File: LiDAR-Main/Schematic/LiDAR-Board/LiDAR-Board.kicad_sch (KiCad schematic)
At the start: 9 parts, among them J1 Conn_01x04, Q1 NPN, Q2 NPN, U1 Pico

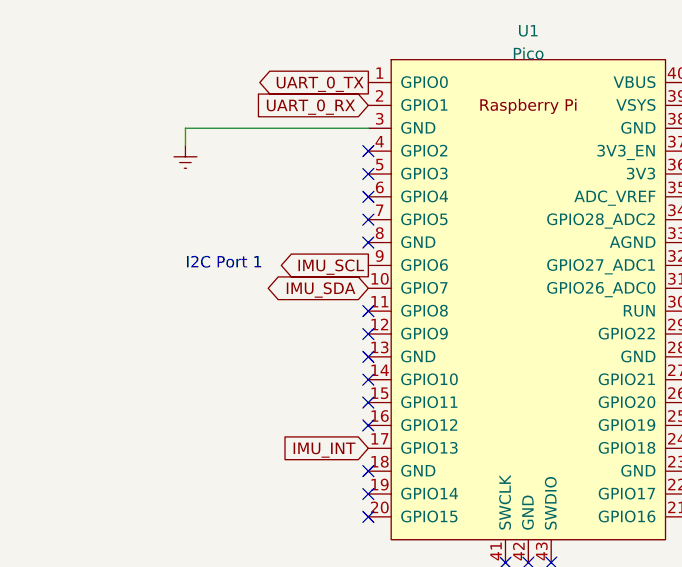
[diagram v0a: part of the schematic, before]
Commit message: Fixed IMU I2C Pin allocation
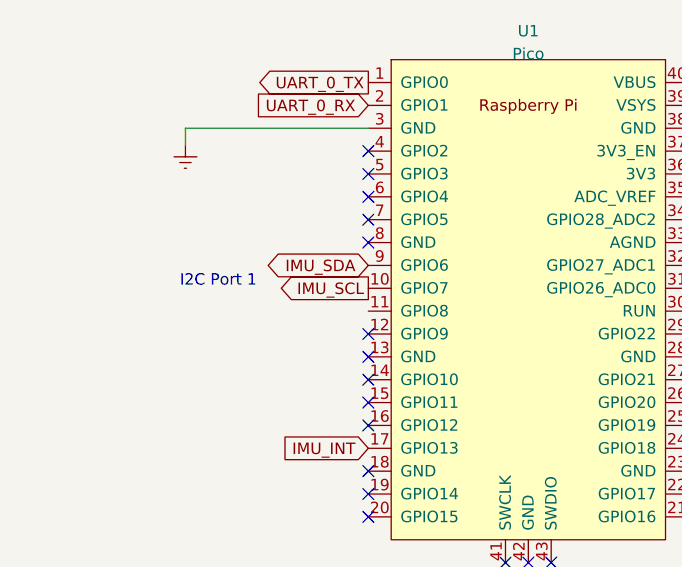
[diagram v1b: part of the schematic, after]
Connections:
- net IMU_SCL: now also U1.10 (GPIO7); no longer U1.9 (GPIO6)
- net IMU_SDA: now also U1.9 (GPIO6); no longer U1.10 (GPIO7)
- no-connect marks 30 -> 29
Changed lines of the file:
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@@
   (no_connect (at 78.74 127.635))
   (no_connect (at 93.98 104.775))
-  (no_connect (at 58.42 99.695))
   (no_connect (at 58.42 112.395))
   (no_connect (at 76.2 127.635))
@@
     (effects (font (size 1.27 1.27)) (justify left bottom))
   )
-  (text "I2C Port 1\n" (at 38.1 95.25 0)
+  (text "I2C Port 1\n" (at 37.465 97.155 0)
     (effects (font (size 1.27 1.27)) (justify left bottom))
   )
@@
     )
   )
-  (global_label "IMU_SDA" (shape bidirectional) (at 58.42 97.155 180) (fields_autoplaced)
-    (effects (font (size 1.27 1.27)) (justify right))
-    (property "Intersheetrefs" "${INTERSHEET_REFS}" (at 46.4805 97.155 0)
+  (global_label "IMU_SDA" (shape bidirectional) (at 58.42 94.615 180) (fields_autoplaced)
+    (effects (font (size 1.27 1.27)) (justify right))
+    (property "Intersheetrefs" "${INTERSHEET_REFS}" (at 46.4805 94.615 0)
       (effects (font (size 1.27 1.27)) (justify right) hide)
     )
@@
     )
   )
-  (global_label "IMU_SCL" (shape output) (at 58.42 94.615 180) (fields_autoplaced)
-    (effects (font (size 1.27 1.27)) (justify right))
-    (property "Intersheetrefs" "${INTERSHEET_REFS}" (at 47.6523 94.615 0)
-      (effects (font (size 1.27 1.27)) (justify right) hide)
-    )
+  (global_label "IMU_SCL" (shape output) (at 58.42 97.155 180) (fields_autoplaced)
+    (effects (font (size 1.27 1.27)) (justify right))
+    (property "Intersheetrefs" "${INTERSHEET_REFS}" (at 47.6523 97.155 0)
+      (effects (font (size 1.27 1.27)) (justify right) hide)
+    )

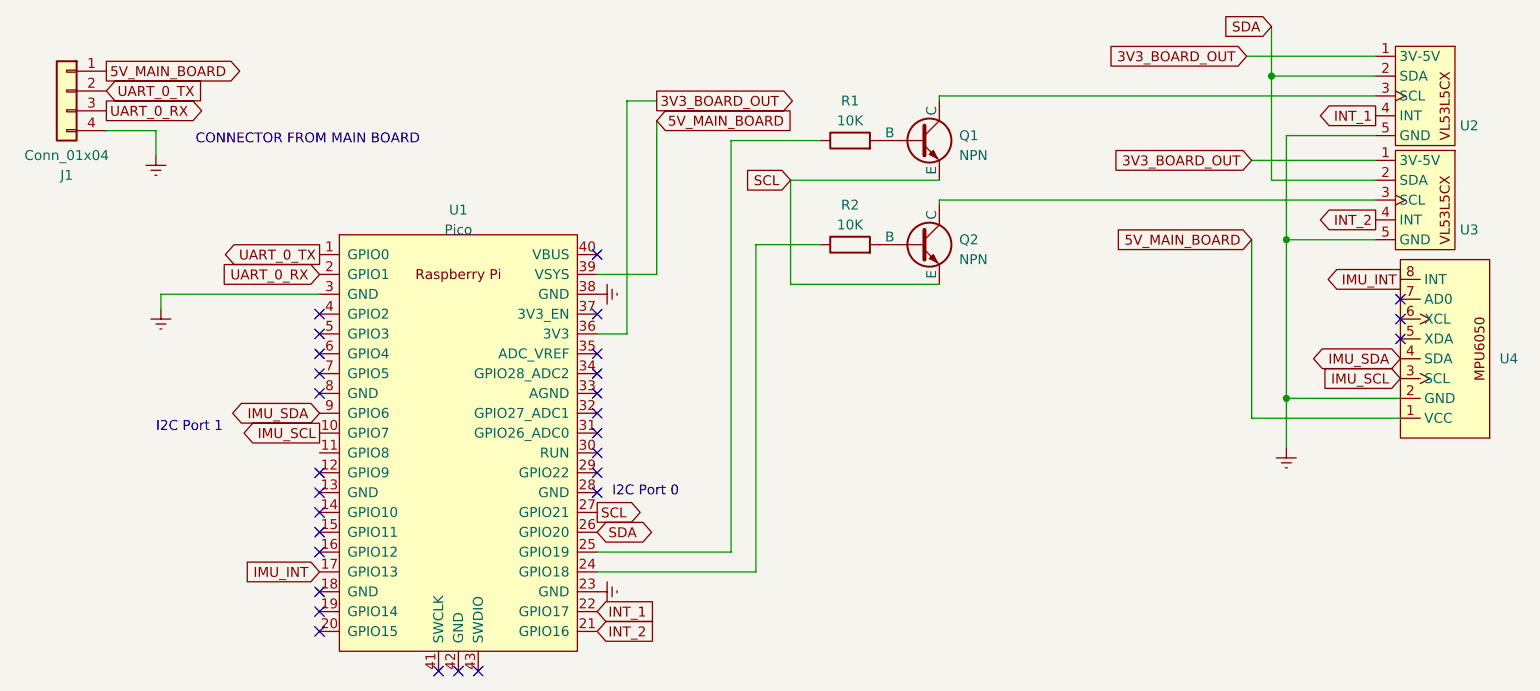
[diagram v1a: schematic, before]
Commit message: Corrected Tx/Rx assignment
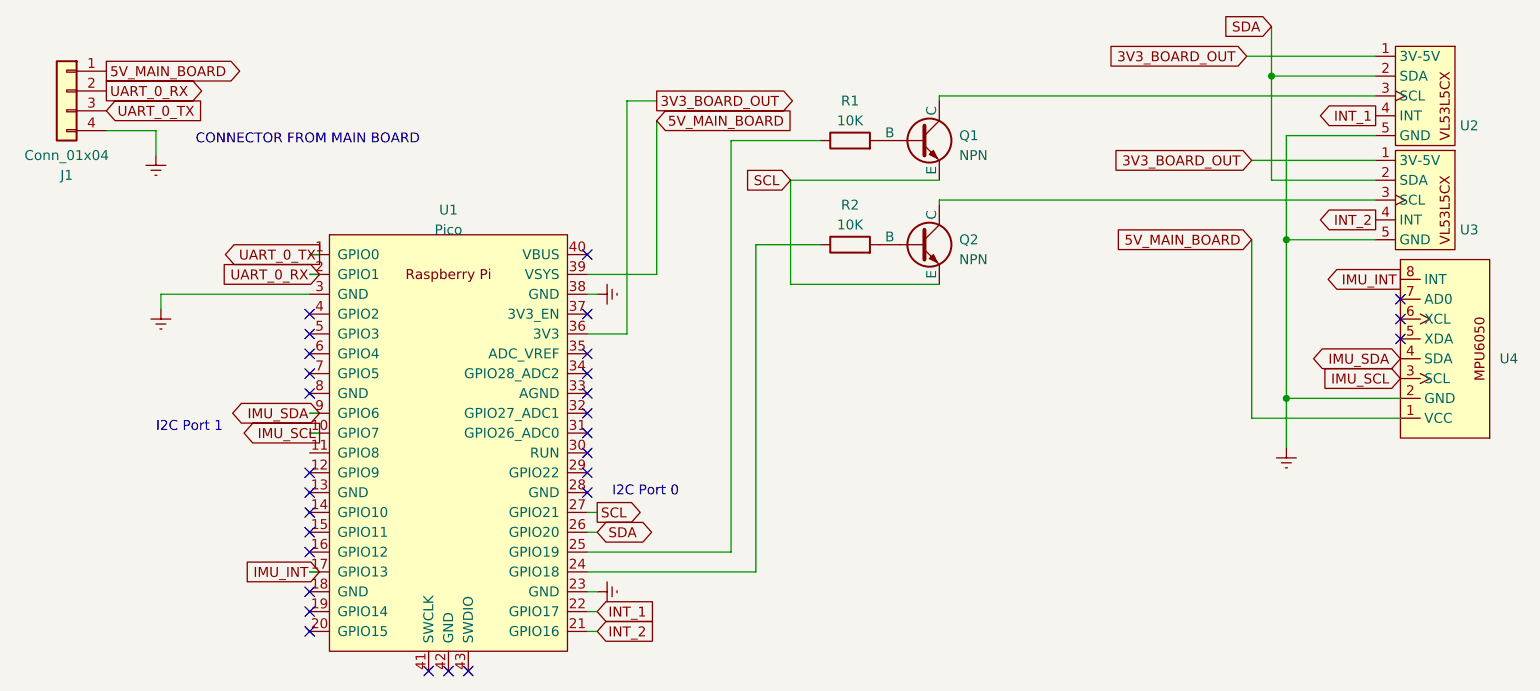
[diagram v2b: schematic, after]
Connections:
- net UART_0_RX: now also J1.2 (Pin_2); no longer J1.3 (Pin_3)
- net UART_0_TX: now also J1.3 (Pin_3); no longer J1.2 (Pin_2)
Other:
- moved on the sheet: U1
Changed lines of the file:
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@@
   (junction (at 182.245 72.39) (diameter 0) (color 0 0 0 0)
   )
-  (no_connect (at 58.42 120.015))
-  (no_connect (at 58.42 92.075))
-  (no_connect (at 58.42 81.915))
-  (no_connect (at 93.98 89.535))
+  (no_connect (at 57.15 120.015))
+  (no_connect (at 57.15 92.075))
+  (no_connect (at 57.15 81.915))
+  (no_connect (at 92.71 89.535))
   (no_connect (at 196.85 80.01))
-  (no_connect (at 93.98 102.235))
-  (no_connect (at 93.98 94.615))
-  (no_connect (at 93.98 99.695))
-  (no_connect (at 58.42 104.775))
-  (no_connect (at 93.98 97.155))
-  (no_connect (at 93.98 74.295))
-  (no_connect (at 58.42 109.855))
-  (no_connect (at 58.42 89.535))
-  (no_connect (at 93.98 86.995))
-  (no_connect (at 58.42 107.315))
+  (no_connect (at 92.71 102.235))
+  (no_connect (at 92.71 94.615))
+  (no_connect (at 92.71 99.695))
+  (no_connect (at 57.15 104.775))
+  (no_connect (at 92.71 97.155))
+  (no_connect (at 92.71 74.295))
+  (no_connect (at 57.15 109.855))
+  (no_connect (at 57.15 89.535))
+  (no_connect (at 92.71 86.995))
+  (no_connect (at 57.15 107.315))
   (no_connect (at 196.85 85.09))
-  (no_connect (at 78.74 127.635))
-  (no_connect (at 93.98 104.775))
-  (no_connect (at 58.42 112.395))
-  (no_connect (at 76.2 127.635))
-  (no_connect (at 73.66 127.635))
-  (no_connect (at 58.42 86.995))
-  (no_connect (at 58.42 102.235))
+  (no_connect (at 77.47 127.635))
+  (no_connect (at 92.71 104.775))
+  (no_connect (at 57.15 112.395))
+  (no_connect (at 74.93 127.635))
+  (no_connect (at 72.39 127.635))
+  (no_connect (at 57.15 86.995))
+  (no_connect (at 57.15 102.235))
   (no_connect (at 196.85 82.55))
-  (no_connect (at 58.42 84.455))
-  (no_connect (at 93.98 92.075))
-  (no_connect (at 93.98 81.915))
-  (no_connect (at 58.42 117.475))
-  (no_connect (at 58.42 122.555))
-  (wire (pts (xy 58.42 79.375) (xy 38.1 79.375))
+  (no_connect (at 57.15 84.455))
+  (no_connect (at 92.71 92.075))
+  (no_connect (at 92.71 81.915))
+  (no_connect (at 57.15 117.475))
+  (no_connect (at 57.15 122.555))
+  (wire (pts (xy 57.15 79.375) (xy 38.1 79.375))
     (stroke (width 0) (type default))
   )
@@
     (stroke (width 0) (type default))
   )
+  (wire (pts (xy 57.15 97.155) (xy 58.42 97.155))
+    (stroke (width 0) (type default))
+  )
   (wire (pts (xy 111.125 112.395) (xy 111.125 59.69))
     (stroke (width 0) (type default))
@@
     (stroke (width 0) (type default))
   )
+  (wire (pts (xy 57.15 74.295) (xy 58.42 74.295))
+    (stroke (width 0) (type default))
+  )
   (wire (pts (xy 114.3 73.025) (xy 114.3 114.935))
     (stroke (width 0) (type default))
@@
     (stroke (width 0) (type default))
   )
-  (wire (pts (xy 114.3 114.935) (xy 93.98 114.935))
+  (wire (pts (xy 57.15 114.935) (xy 58.42 114.935))
+    (stroke (width 0) (type default))
+  )
+  (wire (pts (xy 114.3 114.935) (xy 92.71 114.935))
     (stroke (width 0) (type default))
   )
@@
     (stroke (width 0) (type default))
   )
+  (wire (pts (xy 92.71 117.475) (xy 93.98 117.475))
+    (stroke (width 0) (type default))
+  )
   (wire (pts (xy 118.745 78.105) (xy 137.795 78.105))
     (stroke (width 0) (type default))
@@
     (stroke (width 0) (type default))
   )
-  (wire (pts (xy 93.98 112.395) (xy 111.125 112.395))
+  (wire (pts (xy 92.71 112.395) (xy 111.125 112.395))
     (stroke (width 0) (type default))
   )
@@
     (stroke (width 0) (type default))
   )
+  (wire (pts (xy 92.71 107.315) (xy 93.98 107.315))
+    (stroke (width 0) (type default))
+  )
   (wire (pts (xy 196.85 92.71) (xy 182.245 92.71))
     (stroke (width 0) (type default))
   )
+  (wire (pts (xy 92.71 122.555) (xy 93.98 122.555))
+    (stroke (width 0) (type default))
+  )
   (wire (pts (xy 177.165 48.895) (xy 193.675 48.895))
     (stroke (width 0) (type default))
@@
     (stroke (width 0) (type default))
   )
-  (wire (pts (xy 101.6 76.835) (xy 93.98 76.835))
+  (wire (pts (xy 101.6 76.835) (xy 92.71 76.835))
     (stroke (width 0) (type default))
   )
@@
     (stroke (width 0) (type default))
   )
+  (wire (pts (xy 92.71 109.855) (xy 93.98 109.855))
+    (stroke (width 0) (type default))
+  )
   (wire (pts (xy 180.34 51.435) (xy 180.34 64.77))
     (stroke (width 0) (type default))
@@
     (stroke (width 0) (type default))
   )
-  (wire (pts (xy 93.98 84.455) (xy 97.79 84.455))
+  (wire (pts (xy 92.71 84.455) (xy 97.79 84.455))
     (stroke (width 0) (type default))
   )
@@
     (stroke (width 0) (type default))
   )
+  (wire (pts (xy 57.15 94.615) (xy 58.42 94.615))
+    (stroke (width 0) (type default))
+  )
   (wire (pts (xy 180.34 51.435) (xy 193.675 51.435))
     (stroke (width 0) (type default))
@@
     (stroke (width 0) (type default))
   )
+  (wire (pts (xy 92.71 120.015) (xy 93.98 120.015))
+    (stroke (width 0) (type default))
+  )
   (wire (pts (xy 111.125 59.69) (xy 122.555 59.69))
+    (stroke (width 0) (type default))
+  )
+  (wire (pts (xy 92.71 79.375) (xy 93.98 79.375))
+    (stroke (width 0) (type default))
+  )
+  (wire (pts (xy 57.15 76.835) (xy 58.42 76.835))
     (stroke (width 0) (type default))
   )
@@
     )
   )
-  (global_label "UART_0_RX" (shape output) (at 31.115 55.88 0) (fields_autoplaced)
-    (effects (font (size 1.27 1.27)) (justify left))
-    (property "Intersheetrefs" "${INTERSHEET_REFS}" (at 44.3017 55.88 0)
+  (global_label "UART_0_RX" (shape output) (at 31.115 53.34 0) (fields_autoplaced)
+    (effects (font (size 1.27 1.27)) (justify left))
+    (property "Intersheetrefs" "${INTERSHEET_REFS}" (at 44.3017 53.34 0)
       (effects (font (size 1.27 1.27)) (justify left) hide)
     )
@@
     )
   )
-  (global_label "UART_0_TX" (shape input) (at 31.115 53.34 0) (fields_autoplaced)
-    (effects (font (size 1.27 1.27)) (justify left))
-    (property "Intersheetrefs" "${INTERSHEET_REFS}" (at 43.9993 53.34 0)
+  (global_label "UART_0_TX" (shape input) (at 31.115 55.88 0) (fields_autoplaced)
+    (effects (font (size 1.27 1.27)) (justify left))
+    (property "Intersheetrefs" "${INTERSHEET_REFS}" (at 43.9993 55.88 0)
       (effects (font (size 1.27 1.27)) (justify left) hide)
     )
@@
     )
   )
-  (symbol (lib_id "HEVCS_Sensors:Pico") (at 76.2 98.425 0) (unit 1)
-    (in_bom yes) (on_board yes) (dnp no) (fields_autoplaced)
-    (property "Reference" "U1" (at 76.2 68.58 0)
+  (symbol (lib_id "HEVCS_Sensors:Pico") (at 74.93 98.425 0) (unit 1)
+    (in_bom yes) (on_board yes) (dnp no) (fields_autoplaced)
+    (property "Reference" "U1" (at 74.93 68.58 0)
       (effects (font (size 1.27 1.27)))
     )
-    (property "Value" "Pico" (at 76.2 71.12 0)
+    (property "Value" "Pico" (at 74.93 71.12 0)
       (effects (font (size 1.27 1.27)))
     )
-    (property "Footprint" "HEVCS_Sensor_Footprints:Pi_Pico" (at 76.2 98.425 90)
-      (effects (font (size 1.27 1.27)) hide)
-    )
-    (property "Datasheet" "" (at 76.2 98.425 0)
-      (effects (font (size 1.27 1.27)) hide)
-    )
+    (property "Footprint" "HEVCS_Sensor_Footprints:Pi_Pico" (at 74.93 98.425 90)
+      (effects (font (size 1.27 1.27)) hide)
+    )
+    (property "Datasheet" "" (at 74.93 98.425 0)
+      (effects (font (size 1.27 1.27)) hide)
+    )

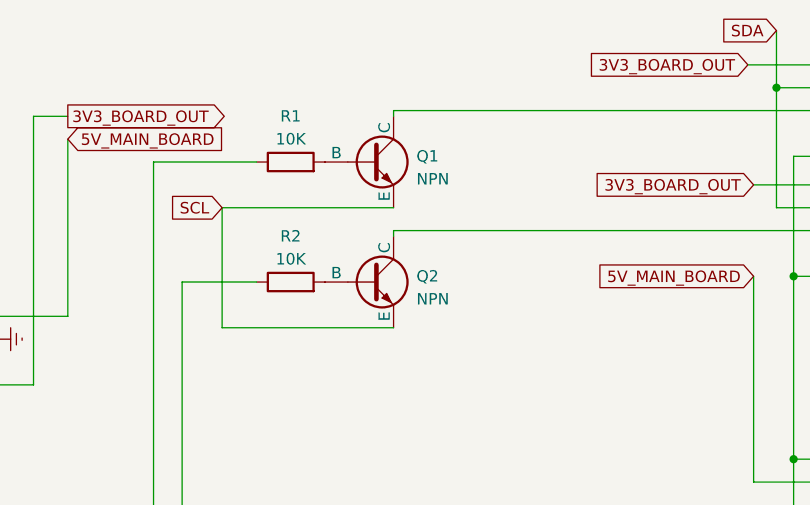
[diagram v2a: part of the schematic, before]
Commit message: Transistor footprint correction - BC817
Replaced generic transistor symbol with the BC817 in a SOT23 package.
Fixed footprint allocation and re-done PCB traces to accomodate change.
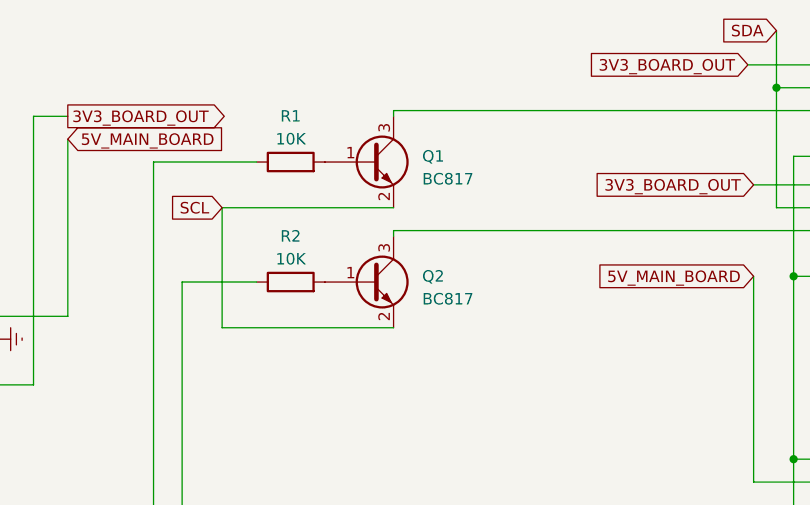
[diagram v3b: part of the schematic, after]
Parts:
- removed Q1, Q2: NPN, Package_TO_SOT_SMD:SOT-23, symbol Simulation_SPICE:NPN
- added Q1, Q2: BC817, Package_TO_SOT_SMD:SOT-23, symbol Transistor_BJT:BC817
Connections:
- net SCL: now also Q1.2 (E), Q2.2 (E)
- net at U2.3 (SCL): now also Q1.3 (C)
- net at R1.2: now also Q1.1 (B)
- net at U3.3 (SCL): now also Q2.3 (C)
- net at R2.2: now also Q2.1 (B)
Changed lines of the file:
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@@
-    )
-  )
-  (symbol (lib_id "Simulation_SPICE:NPN") (at 135.255 59.69 0) (unit 1)
-    (in_bom yes) (on_board yes) (dnp no) (fields_autoplaced)
-    (property "Reference" "Q1" (at 140.335 59.055 0)
-      (effects (font (size 1.27 1.27)) (justify left))
-    )
-    (property "Value" "NPN" (at 140.335 61.595 0)
-      (effects (font (size 1.27 1.27)) (justify left))
-    )
-    (property "Footprint" "Package_TO_SOT_SMD:SOT-23" (at 198.755 59.69 0)
-      (effects (font (size 1.27 1.27)) hide)
-    )
-    (property "Datasheet" "~" (at 198.755 59.69 0)
-      (effects (font (size 1.27 1.27)) hide)
-    )
-    (property "Sim.Device" "NPN" (at 135.255 59.69 0)
-      (effects (font (size 1.27 1.27)) hide)
-    )
-    (property "Sim.Type" "GUMMELPOON" (at 135.255 59.69 0)
-      (effects (font (size 1.27 1.27)) hide)
-    )
-    (property "Sim.Pins" "1=C 2=B 3=E" (at 135.255 59.69 0)
-      (effects (font (size 1.27 1.27)) hide)
-    )
-    (pin "1")
-    (pin "2")
-    (pin "3")
-    (instances
-      (project "LiDAR-Board"
-        (path "/379f291a-31d3-4ed1-aaf1-b1b6ffabef49"
-          (reference "Q1") (unit 1)
-        )
-      )
-    )
-  )
-  (symbol (lib_id "Simulation_SPICE:NPN") (at 135.255 73.025 0) (unit 1)
-    (in_bom yes) (on_board yes) (dnp no) (fields_autoplaced)
-    (property "Reference" "Q2" (at 140.335 72.39 0)
-      (effects (font (size 1.27 1.27)) (justify left))
-    )
-    (property "Value" "NPN" (at 140.335 74.93 0)
-      (effects (font (size 1.27 1.27)) (justify left))
-    )
-    (property "Footprint" "Package_TO_SOT_SMD:SOT-23" (at 198.755 73.025 0)
-      (effects (font (size 1.27 1.27)) hide)
-    )
-    (property "Datasheet" "~" (at 198.755 73.025 0)
-      (effects (font (size 1.27 1.27)) hide)
-    )
-    (property "Sim.Device" "NPN" (at 135.255 73.025 0)
-      (effects (font (size 1.27 1.27)) hide)
-    )
-    (property "Sim.Type" "GUMMELPOON" (at 135.255 73.025 0)
-      (effects (font (size 1.27 1.27)) hide)
-    )
-    (property "Sim.Pins" "1=C 2=B 3=E" (at 135.255 73.025 0)
-      (effects (font (size 1.27 1.27)) hide)
-    )
-    (pin "1")
-    (pin "2")
-    (pin "3")
-    (instances
-      (project "LiDAR-Board"
-        (path "/379f291a-31d3-4ed1-aaf1-b1b6ffabef49"
-          (reference "Q2") (unit 1)
-        )
-      )
     )
   )
@@
     )
   )
+  (symbol (lib_id "Transistor_BJT:BC817") (at 135.255 73.025 0) (unit 1)
+    (in_bom yes) (on_board yes) (dnp no) (fields_autoplaced)
+    (property "Reference" "Q2" (at 140.97 72.39 0)
+      (effects (font (size 1.27 1.27)) (justify left))
+    )
+    (property "Value" "BC817" (at 140.97 74.93 0)
+      (effects (font (size 1.27 1.27)) (justify left))
+    )
+    (property "Footprint" "Package_TO_SOT_SMD:SOT-23" (at 140.335 74.93 0)
+      (effects (font (size 1.27 1.27) italic) (justify left) hide)
+    )
+    (property "Datasheet" "https://www.onsemi.com/pub/Collateral/BC818-D.pdf" (at 135.255 73.025 0)
+      (effects (font (size 1.27 1.27)) (justify left) hide)
+    )
+    (pin "1")
+    (pin "2")
+    (pin "3")
+    (instances
+      (project "LiDAR-Board"
+        (path "/379f291a-31d3-4ed1-aaf1-b1b6ffabef49"
+          (reference "Q2") (unit 1)
+        )
+      )
+    )
+  )
   (symbol (lib_id "Connector_Generic:Conn_01x04") (at 26.035 53.34 0) (mirror y) (unit 1)
     (in_bom yes) (on_board yes) (dnp no)
@@
         )
       )
+    )
+  )
+  (symbol (lib_id "Transistor_BJT:BC817") (at 135.255 59.69 0) (unit 1)
+    (in_bom yes) (on_board yes) (dnp no) (fields_autoplaced)
+    (property "Reference" "Q1" (at 140.97 59.055 0)
+      (effects (font (size 1.27 1.27)) (justify left))
+    )
+    (property "Value" "BC817" (at 140.97 61.595 0)
+      (effects (font (size 1.27 1.27)) (justify left))
+    )
+    (property "Footprint" "Package_TO_SOT_SMD:SOT-23" (at 140.335 61.595 0)
+      (effects (font (size 1.27 1.27) italic) (justify left) hide)
+    )
+    (property "Datasheet" "https://www.onsemi.com/pub/Collateral/BC818-D.pdf" (at 135.255 59.69 0)
+      (effects (font (size 1.27 1.27)) (justify left) hide)
+    )
+    (pin "1")
+    (pin "2")
+    (pin "3")
+    (instances
+      (project "LiDAR-Board"
+        (path "/379f291a-31d3-4ed1-aaf1-b1b6ffabef49"
+          (reference "Q1") (unit 1)
+        )
+      )
